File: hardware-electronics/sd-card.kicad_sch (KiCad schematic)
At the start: 40 parts, among them J5 Micro_SD_Card_Det_Hirose_DM3AT, J8 TC2030-IDC-NL, U6 24AA04T-I_OT, U9 USB2244-AEZG-06, Y3 ECS-240-10-47-CKM-TR

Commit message: [#26] Correct MPN GRM155R61H105KE05D
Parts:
- C26, C28, C30, C32, C34, C36, C37, C6: Author Your Name -> Lukasz Nowarkiewicz; MPN GRM155R61H105KE92D -> GRM155R61H105KE05D
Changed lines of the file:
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@@
 			)
 		)
-		(property "MPN" "GRM155R61H105KE92D"
+		(property "MPN" "GRM155R61H105KE05D"
 			(at 210.82 86.36 0)
 			(effects
@@
 			)
 		)
-		(property "Author" "Your Name"
+		(property "Author" "Lukasz Nowarkiewicz"
 			(at 218.44 86.36 0)
 			(effects
@@
 			)
 		)
-		(property "MPN" "GRM155R61H105KE92D"
+		(property "MPN" "GRM155R61H105KE05D"
 			(at 95.25 60.96 0)
 			(effects
@@
 			)
 		)
-		(property "Author" "Your Name"
+		(property "Author" "Lukasz Nowarkiewicz"
 			(at 102.87 60.96 0)
 			(effects
@@
 			)
 		)
-		(property "MPN" "GRM155R61H105KE92D"
+		(property "MPN" "GRM155R61H105KE05D"
 			(at 105.41 35.56 0)
 			(effects
@@
 			)
 		)
-		(property "Author" "Your Name"
+		(property "Author" "Lukasz Nowarkiewicz"
 			(at 113.03 35.56 0)
 			(effects
@@
 			)
 		)
-		(property "MPN" "GRM155R61H105KE92D"
+		(property "MPN" "GRM155R61H105KE05D"
 			(at 276.86 74.93 0)
 			(effects
@@
 			)
 		)
-		(property "Author" "Your Name"
+		(property "Author" "Lukasz Nowarkiewicz"
 			(at 284.48 74.93 0)
 			(effects
@@
 			)
 		)
-		(property "MPN" "GRM155R61H105KE92D"
+		(property "MPN" "GRM155R61H105KE05D"
 			(at 293.37 68.58 0)
 			(effects
@@
 			)
 		)
-		(property "Author" "Your Name"
+		(property "Author" "Lukasz Nowarkiewicz"
 			(at 300.99 68.58 0)
 			(effects
@@
 			)
 		)
-		(property "MPN" "GRM155R61H105KE92D"
+		(property "MPN" "GRM155R61H105KE05D"
 			(at 254 78.74 0)
 			(effects
@@
 			)
 		)
-		(property "Author" "Your Name"
+		(property "Author" "Lukasz Nowarkiewicz"
 			(at 261.62 78.74 0)
 			(effects
@@
 			)
 		)
-		(property "MPN" "GRM155R61H105KE92D"
+		(property "MPN" "GRM155R61H105KE05D"
 			(at 101.6 154.94 0)
 			(effects
@@
 			)
 		)
-		(property "Author" "Your Name"
+		(property "Author" "Lukasz Nowarkiewicz"
 			(at 109.22 154.94 0)
 			(effects
@@
 			)
 		)
-		(property "MPN" "GRM155R61H105KE92D"
+		(property "MPN" "GRM155R61H105KE05D"
 			(at 236.22 78.74 0)
 			(effects
@@
 			)
 		)
-		(property "Author" "Your Name"
+		(property "Author" "Lukasz Nowarkiewicz"
 			(at 243.84 78.74 0)
 			(effects

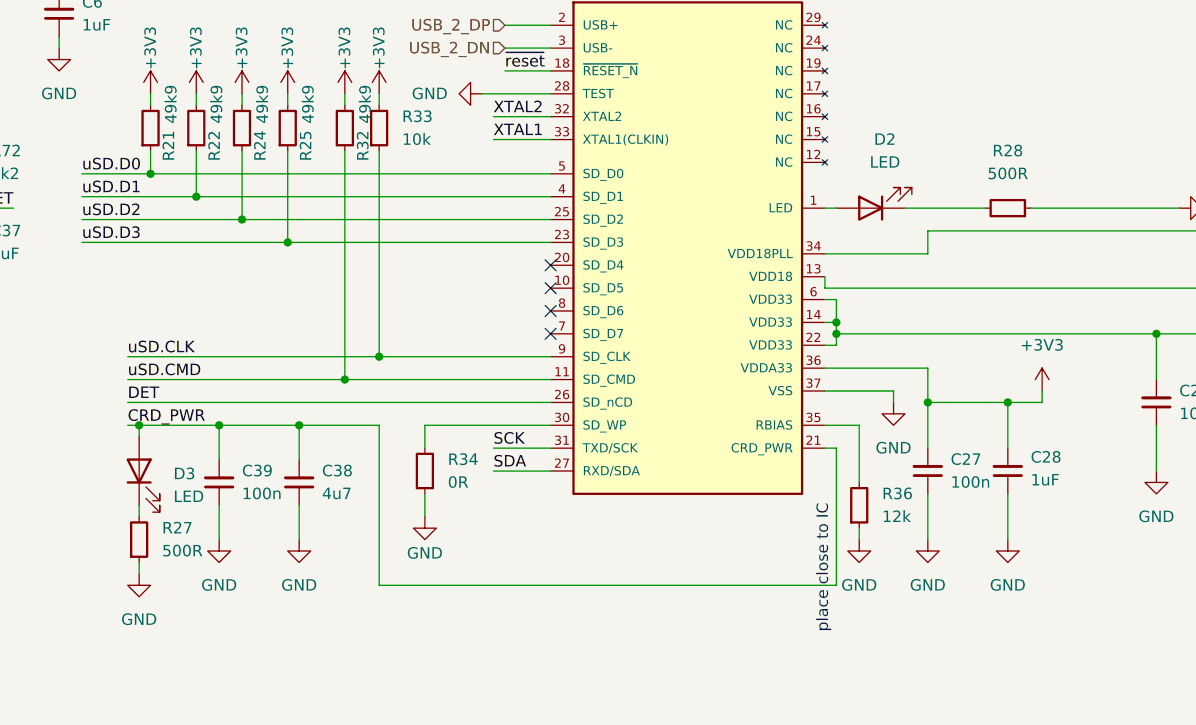
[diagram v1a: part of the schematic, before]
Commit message: [#26] Replace 500ohm to 510ohm  MPN CRCW0402510RJNED
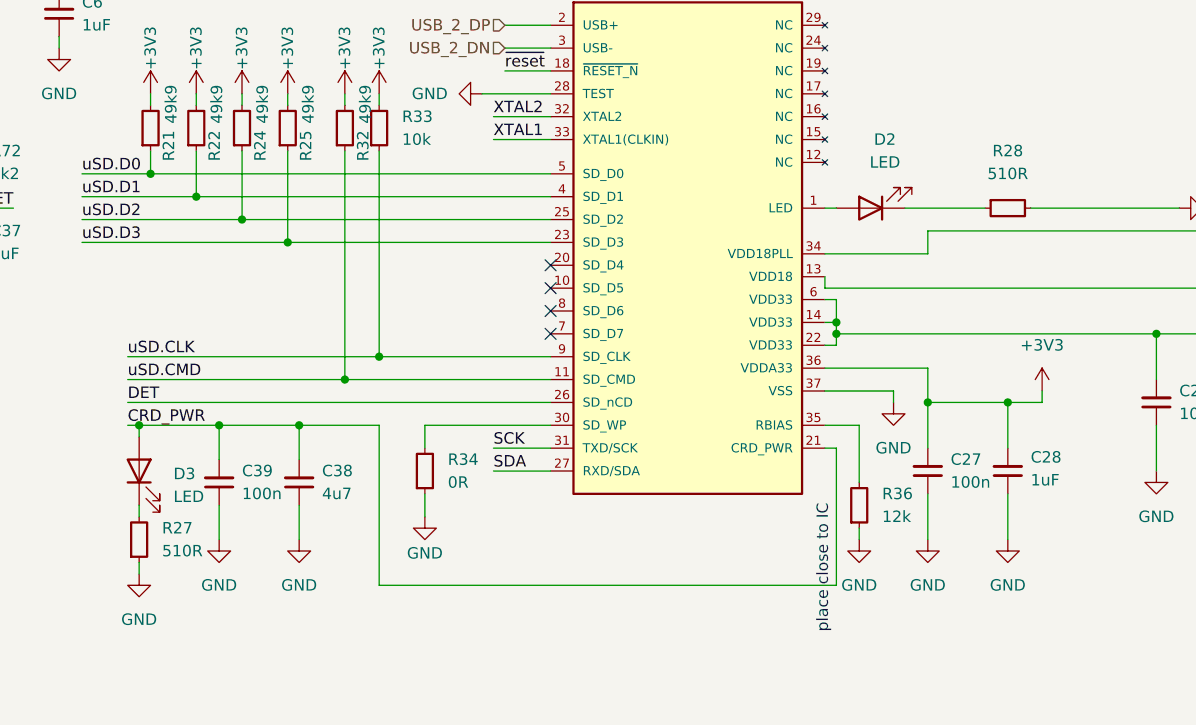
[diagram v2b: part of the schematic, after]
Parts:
- removed R27, R28: R_500R_0402, M2SmartHomeFootprints:R_0402, symbol M2SmartHomeSymbols:R_500R_0402
- added R27, R28: R_510R_0402, M2SmartHomeFootprints:R_0402, symbol M2SmartHomeSymbols:R_510R_0402
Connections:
- net GND: now also R27.1, R28.2
- net at D3.1 (K): now also R27.2
- net at D2.1 (K): now also R28.1

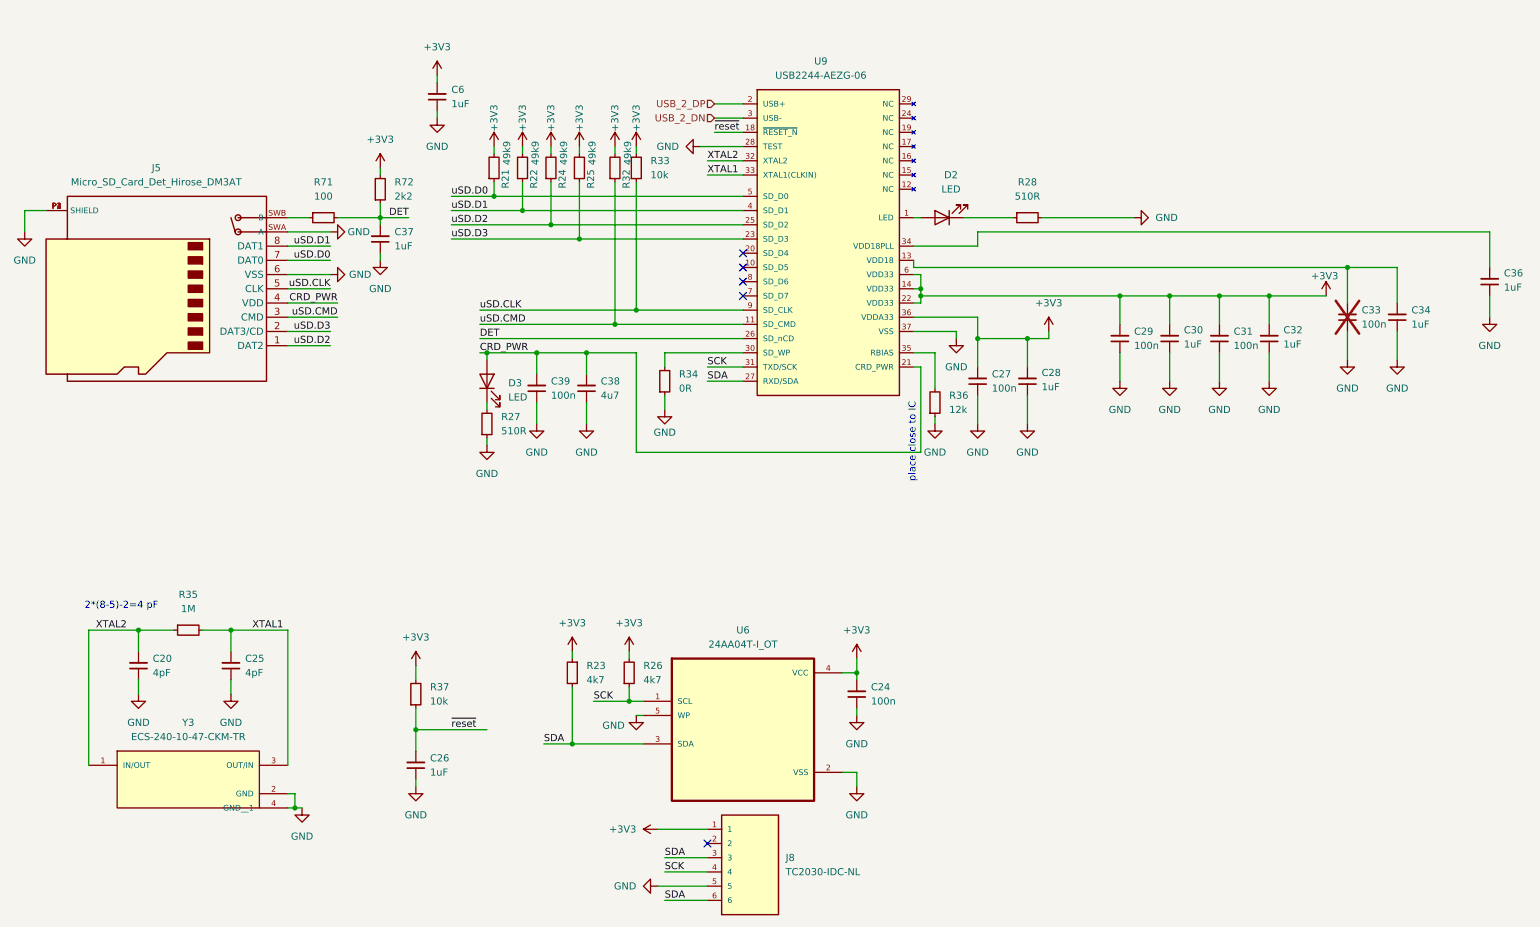
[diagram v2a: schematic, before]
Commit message: [#26] Add I2C EEPROM for emmc and usd ICP
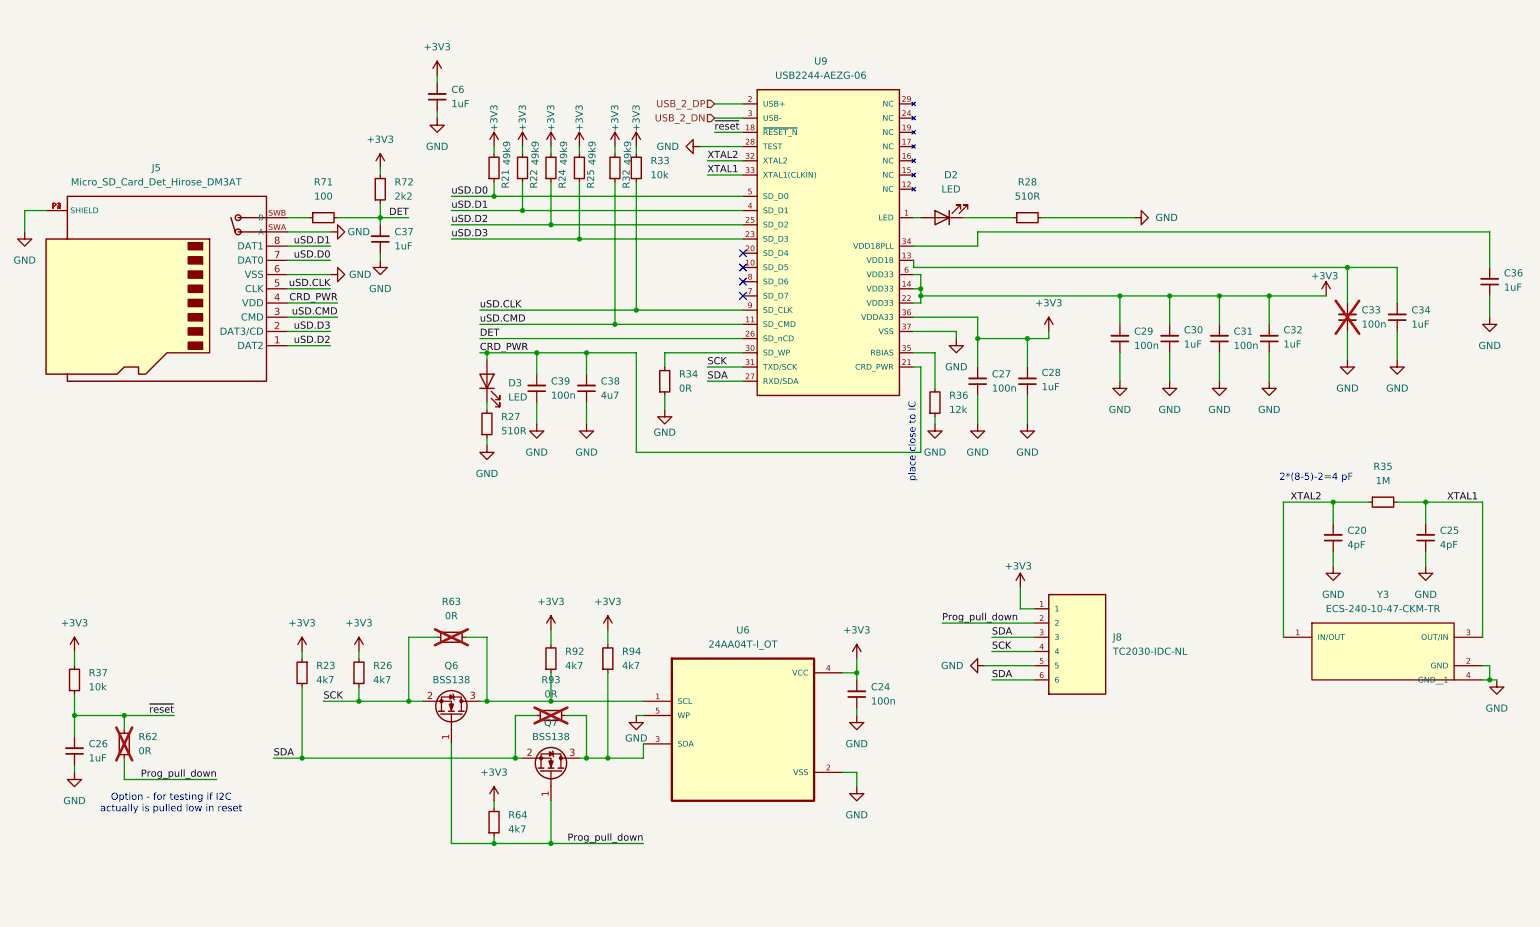
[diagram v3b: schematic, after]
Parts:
- added Q6, Q7: BSS138, Package_TO_SOT_SMD:SOT-23, symbol Transistor_FET:BSS138
- added R62, R63, R93: R_0_0402, M2SmartHomeFootprints:R_0402, symbol M2SmartHomeSymbols:R_0_0402
- added R64, R92, R94: R_4k7_0402, M2SmartHomeFootprints:R_0402, symbol M2SmartHomeSymbols:R_4k7_0402
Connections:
- net +3V3: now also R64.2, R92.2, R94.2
- net SCK: now also Q6.2 (S), R63.2; no longer U6.1 (SCL)
- net SDA: now also Q7.2 (S), R93.2; no longer U6.3 (SDA)
- net ~{reset}: now also R62.1
- net Prog_pull_down: now reaches J8.2
- net Prog_pull_down: now also Q6.1 (G), Q7.1 (G), R62.2, R64.1
- new net: Q7.3 (D), R93.1, R94.1, U6.3 (SDA)
- new net: Q6.3 (D), R63.1, R92.1, U6.1 (SCL)
- no-connect marks 5 -> 4
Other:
- note added: "Option - for testing if I2C actually is pulled low in reset"
- moved on the sheet: C20, C25, C26, J8, R23, R26, R35, R37, Y3

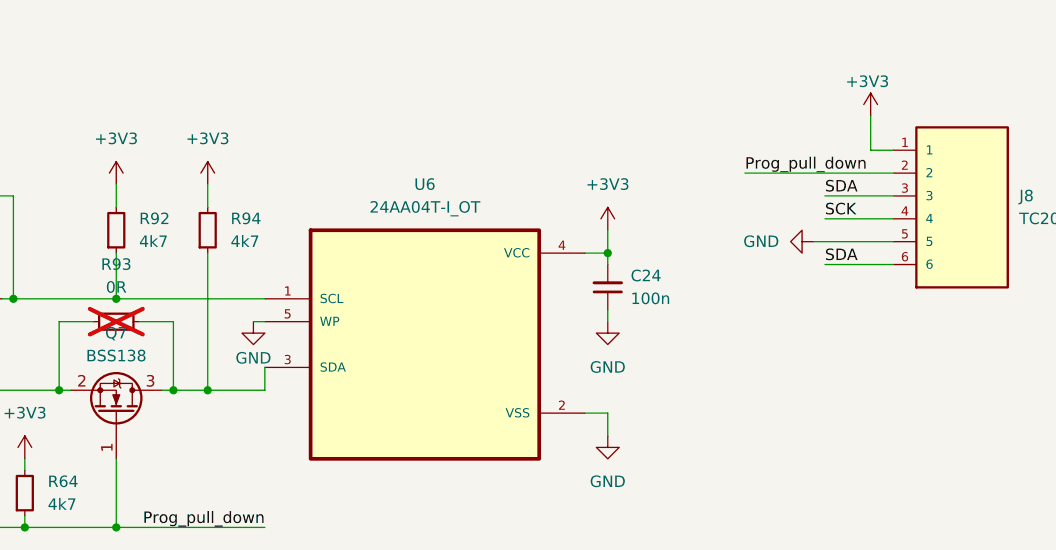
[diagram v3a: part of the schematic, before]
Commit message: [#26] Fix connections to TC2030 I2C
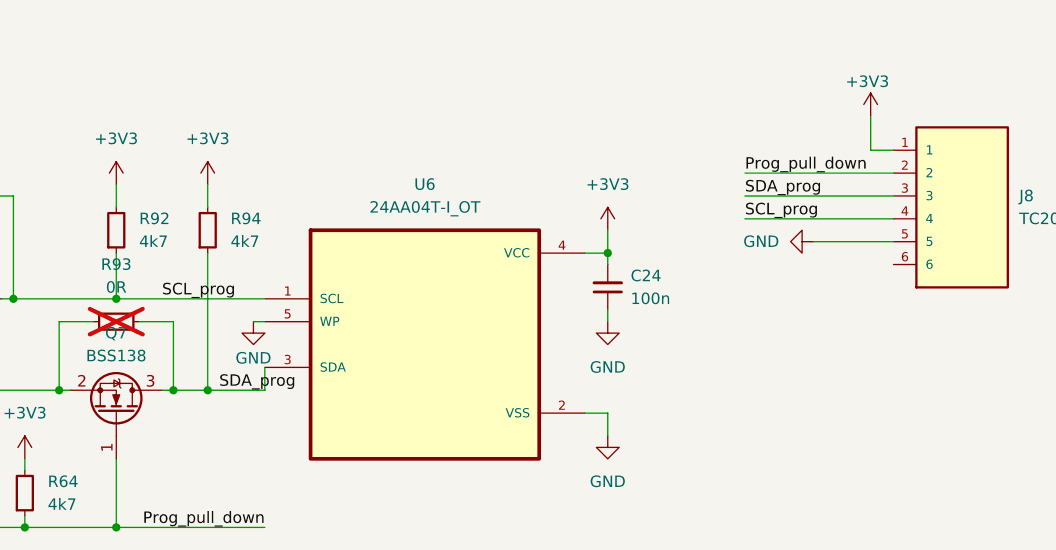
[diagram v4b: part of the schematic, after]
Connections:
- net SCK: no longer J8.4
- net SDA: no longer J8.3, J8.6
- net SDA_prog: now reaches Q7.3 (D), R93.1, R94.1, U6.3 (SDA)
- net SDA_prog: now also J8.3
- net SCL_prog: now reaches Q6.3 (D), R63.1, R92.1, U6.1 (SCL)
- net SCL_prog: now also J8.4
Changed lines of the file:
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@@
-	(wire
-		(pts
-			(xy 186.69 152.4) (xy 194.31 152.4)
-		)
-		(stroke
-			(width 0)
-			(type default)
-		)
-	)
 	(wire
 		(pts
@@
 	(wire
 		(pts
+			(xy 177.8 152.4) (xy 194.31 152.4)
+		)
+		(stroke
+			(width 0)
+			(type default)
+		)
+	)
+	(wire
+		(pts
 			(xy 185.42 154.94) (xy 194.31 154.94)
 		)
@@
 	(wire
 		(pts
+			(xy 177.8 149.86) (xy 194.31 149.86)
+		)
+		(stroke
+			(width 0)
+			(type default)
+		)
+	)
+	(wire
+		(pts
 			(xy 275.59 88.9) (xy 275.59 92.71)
 		)
@@
 	(wire
 		(pts
-			(xy 186.69 157.48) (xy 194.31 157.48)
-		)
-		(stroke
-			(width 0)
-			(type default)
-		)
-	)
-	(wire
-		(pts
 			(xy 123.19 116.84) (xy 123.19 99.06)
 		)
@@
 		(pts
 			(xy 184.15 96.52) (xy 193.04 96.52)
-		)
-		(stroke
-			(width 0)
-			(type default)
-		)
-	)
-	(wire
-		(pts
-			(xy 186.69 149.86) (xy 194.31 149.86)
 		)
 		(stroke
@@
 		)
 	)
-	(label "SDA"
-		(at 186.69 149.86 0)
-		(fields_autoplaced yes)
-		(effects
-			(font
-				(size 1.27 1.27)
-			)
-			(justify left bottom)
-		)
-	)
 	(label "XTAL1"
 		(at 135.89 67.31 0)
@@
 		)
 	)
+	(label "SCL_prog"
+		(at 113.03 161.29 0)
+		(fields_autoplaced yes)
+		(effects
+			(font
+				(size 1.27 1.27)
+			)
+			(justify left bottom)
+		)
+	)
 	(label "SCK"
 		(at 67.31 161.29 0)
@@
 		)
 	)
+	(label "SDA_prog"
+		(at 177.8 149.86 0)
+		(fields_autoplaced yes)
+		(effects
+			(font
+				(size 1.27 1.27)
+			)
+			(justify left bottom)
+		)
+	)
 	(label "DET"
 		(at 95.25 96.52 0)
@@
 		)
 	)
+	(label "SCL_prog"
+		(at 177.8 152.4 0)
+		(fields_autoplaced yes)
+		(effects
+			(font
+				(size 1.27 1.27)
+			)
+			(justify left bottom)
+		)
+	)
 	(label "uSD.CLK"
 		(at 68.58 87.63 180)
@@
 		)
 	)
+	(label "SDA_prog"
+		(at 119.38 171.45 0)
+		(fields_autoplaced yes)
+		(effects
+			(font
+				(size 1.27 1.27)
+			)
+			(justify left bottom)
+		)
+	)
 	(label "uSD.D1"
 		(at 90.17 73.66 0)
@@
 		)
 	)
-	(label "SDA"
-		(at 186.69 157.48 0)
-		(fields_autoplaced yes)
-		(effects
-			(font
-				(size 1.27 1.27)
-			)
-			(justify left bottom)
-		)
-	)
 	(label "uSD.D0"
 		(at 68.58 82.55 180)
@@
 		(fields_autoplaced yes)
 		(effects
-			(font
-				(size 1.27 1.27)
-			)
-			(justify left bottom)
-		)
-	)
-	(label "SCK"
-		(at 186.69 152.4 0)
-		(fields_autoplaced yes)
-		(effects

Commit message: TC2030-IDC-NL exclude from BOM
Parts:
- J8: now left out of the parts list
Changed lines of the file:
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@@
 		(unit 1)
 		(exclude_from_sim no)
-		(in_bom yes)
+		(in_bom no)
 		(on_board yes)
 		(dnp no)

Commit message: ECS-240-10-47-CKM-TR add MPN
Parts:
- Y3: MPN (none) -> ECS-240-10-47-CKM-TR
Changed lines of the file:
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@@
+			)
+		)
+		(property "MPN" "ECS-240-10-47-CKM-TR"
+			(at 256.54 152.4 0)
+			(effects
+				(font
+					(size 1.27 1.27)
+				)
+				(hide yes)
 			)
 		)

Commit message: DM3AT-SF-PEJM5 add MPN
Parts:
- J5: MPN (none) -> DM3AT-SF-PEJM5; Manufacturer (none) -> Hirose
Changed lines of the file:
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@@
+			)
+		)
+		(property "Manufacturer" "Hirose"
+			(at 38.1 87.63 0)
+			(effects
+				(font
+					(size 1.27 1.27)
+				)
+				(hide yes)
+			)
+		)
+		(property "MPN" "DM3AT-SF-PEJM5"
+			(at 38.1 87.63 0)
+			(effects
+				(font
+					(size 1.27 1.27)
+				)
+				(hide yes)
 			)
 		)
